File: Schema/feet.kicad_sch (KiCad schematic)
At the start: 15 parts, among them U4 Accelerometer

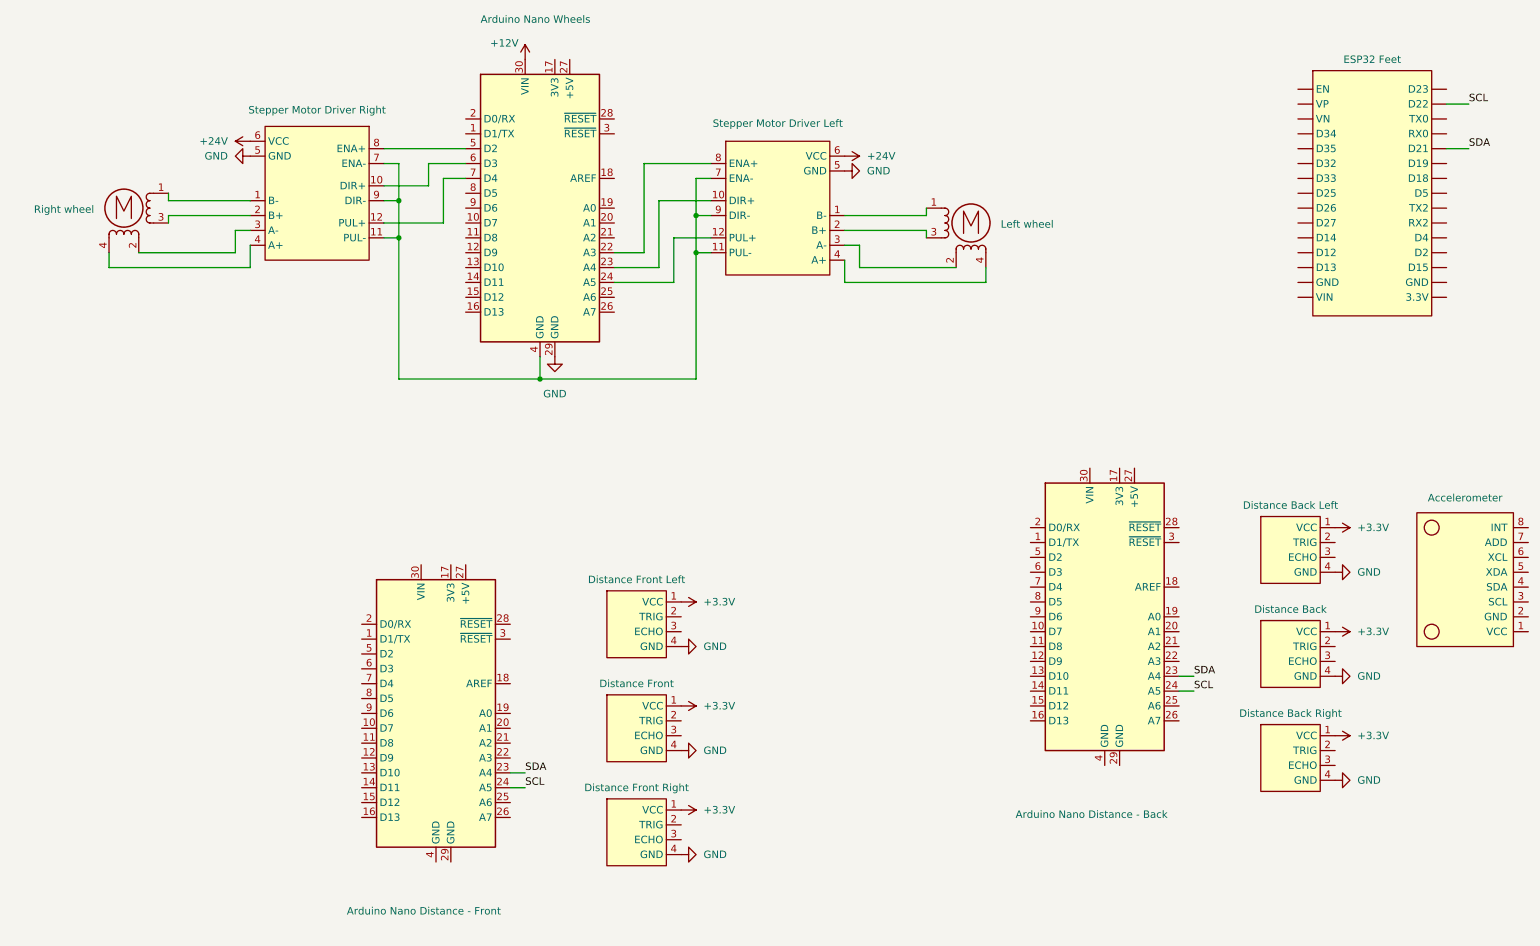
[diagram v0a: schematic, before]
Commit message: Updated schema and added math before ONCS
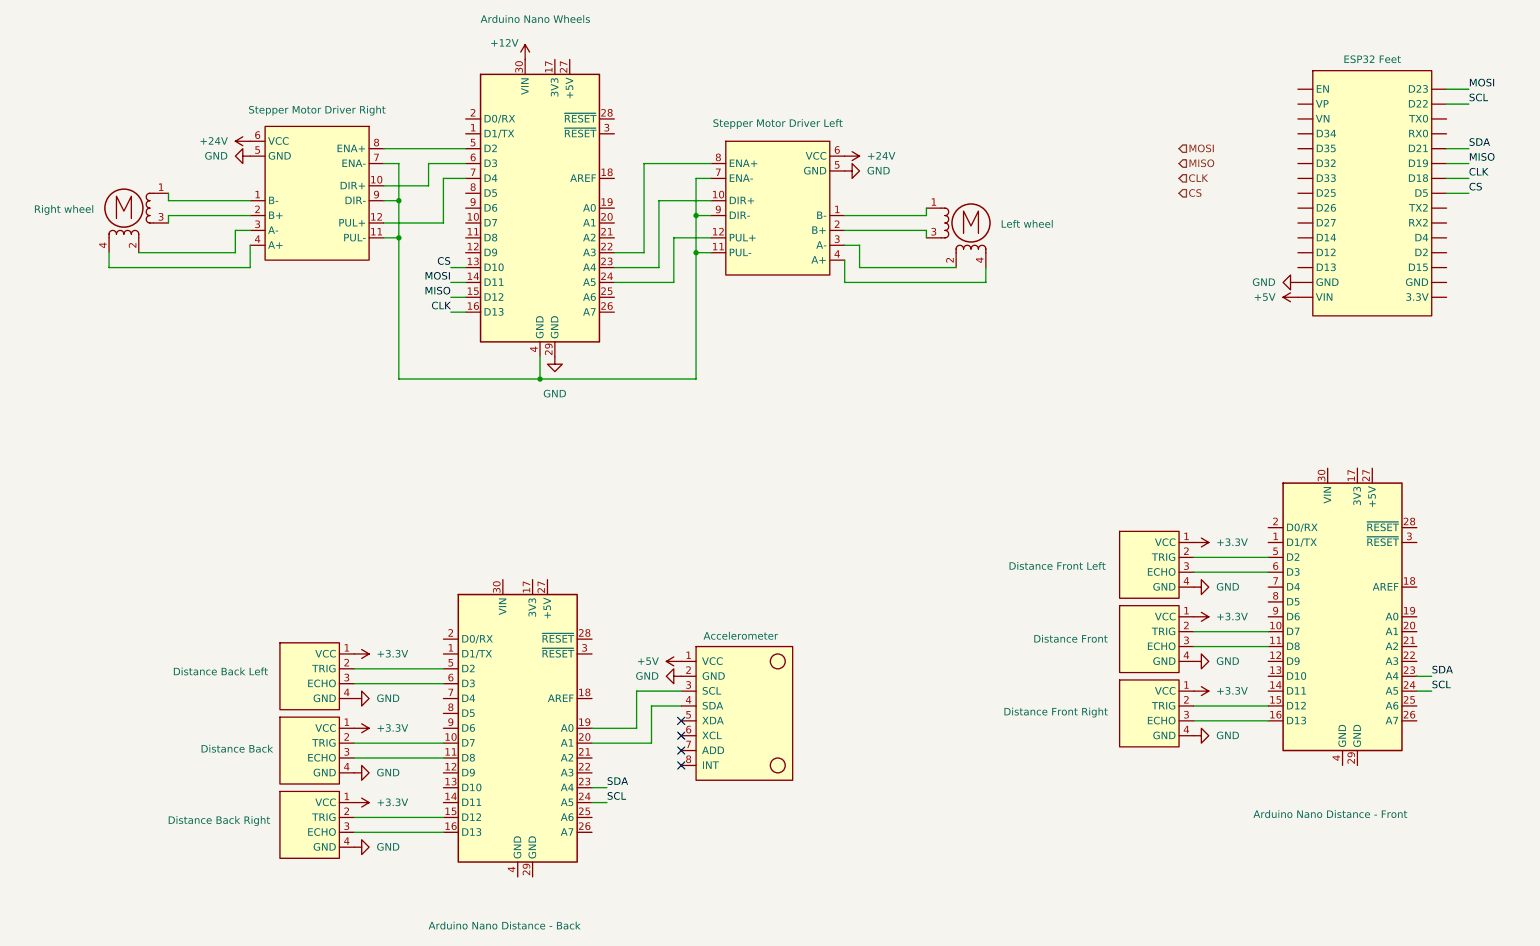
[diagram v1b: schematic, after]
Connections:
- net GND: now also ESP32 DEV KIT v3. (VP), U4.2 (GND)
- net at Ultrasonic sensor2.2 (TRIG): now also A5.10 (D7)
- net at Ultrasonic sensor2.3 (ECHO): now also A5.11 (D8)
- net at A5.15 (D12): now also Ultrasonic sensor3.2 (TRIG)
- net at A5.16 (D13): now also Ultrasonic sensor3.3 (ECHO)
- net at A5.5 (D2): now also Ultrasonic sensor1.2 (TRIG)
- net at A5.6 (D3): now also Ultrasonic sensor1.3 (ECHO)
- net CS: now reaches A1.13 (D10)
- net CS: now also ESP32 DEV KIT v3. (VP)
- net MOSI: now reaches A1.14 (D11)
- net MOSI: now also ESP32 DEV KIT v3. (VP)
- net MISO: now reaches A1.15 (D12)
- net MISO: now also ESP32 DEV KIT v3. (VP)
- net CLK: now reaches A1.16 (D13)
- net CLK: now also ESP32 DEV KIT v3. (VP)
- net at Ultrasonic sensor6.2 (TRIG): now also A4.15 (D12)
- net at Ultrasonic sensor6.3 (ECHO): now also A4.16 (D13)
- net at Ultrasonic sensor4.2 (TRIG): now also A4.5 (D2)
- net at Ultrasonic sensor4.3 (ECHO): now also A4.6 (D3)
- net at Ultrasonic sensor5.2 (TRIG): now also A4.10 (D7)
- net at Ultrasonic sensor5.3 (ECHO): now also A4.11 (D8)
- net +5V: now reaches U4.1 (VCC)
- net +5V: now also ESP32 DEV KIT v3. (VP)
- net at U4.3 (SCL): now also A4.19 (A0)
- net at U4.4 (SDA): now also A4.20 (A1)
- no-connect marks 0 -> 4
